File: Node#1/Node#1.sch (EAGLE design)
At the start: 5 parts, among them U1 BLUENRG-232

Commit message: Modified Lib, Node#1
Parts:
- added C10, C4, C5, C6, C7, C8, C9: (no value), rcl:C-EUC0805K
- added C11: (no value), rcl:C-EUC0805
- added D1: BAS40-06, diode:BAS40-06
- added R1, R2: (no value), rcl:R-EU_R0805
- added S1: FSM4JSMAATR, BlueHome:FSM4JSMAATR
- added U$2: SWITCH_L, BlueHome:SWITCH_L
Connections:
- new net N$1: C7.1, C8.1, U1.VDD1V2
- new net N$2: C10.1, C9.1, U$2.1, U1.SMPSFILT1
- new net N$3: C11.2, D1.AA, R1.1, S1.3, S1.4, U1.RESETN
- new net N$5: C11.1, R2.1, S1.1, S1.2
- new net SMPSFILT2: U$2.2, U1.SMPSFILT2
- net +3V3: now also C4.1, C5.1, C6.1, D1.K2, R1.2, U$2.3
- net 0V: now also C10.2, C4.2, C5.2, C6.2, C7.2, C8.2, C9.2, R2.2; no longer U1.VDD1V2
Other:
- moved on the sheet: C1, C2, C3

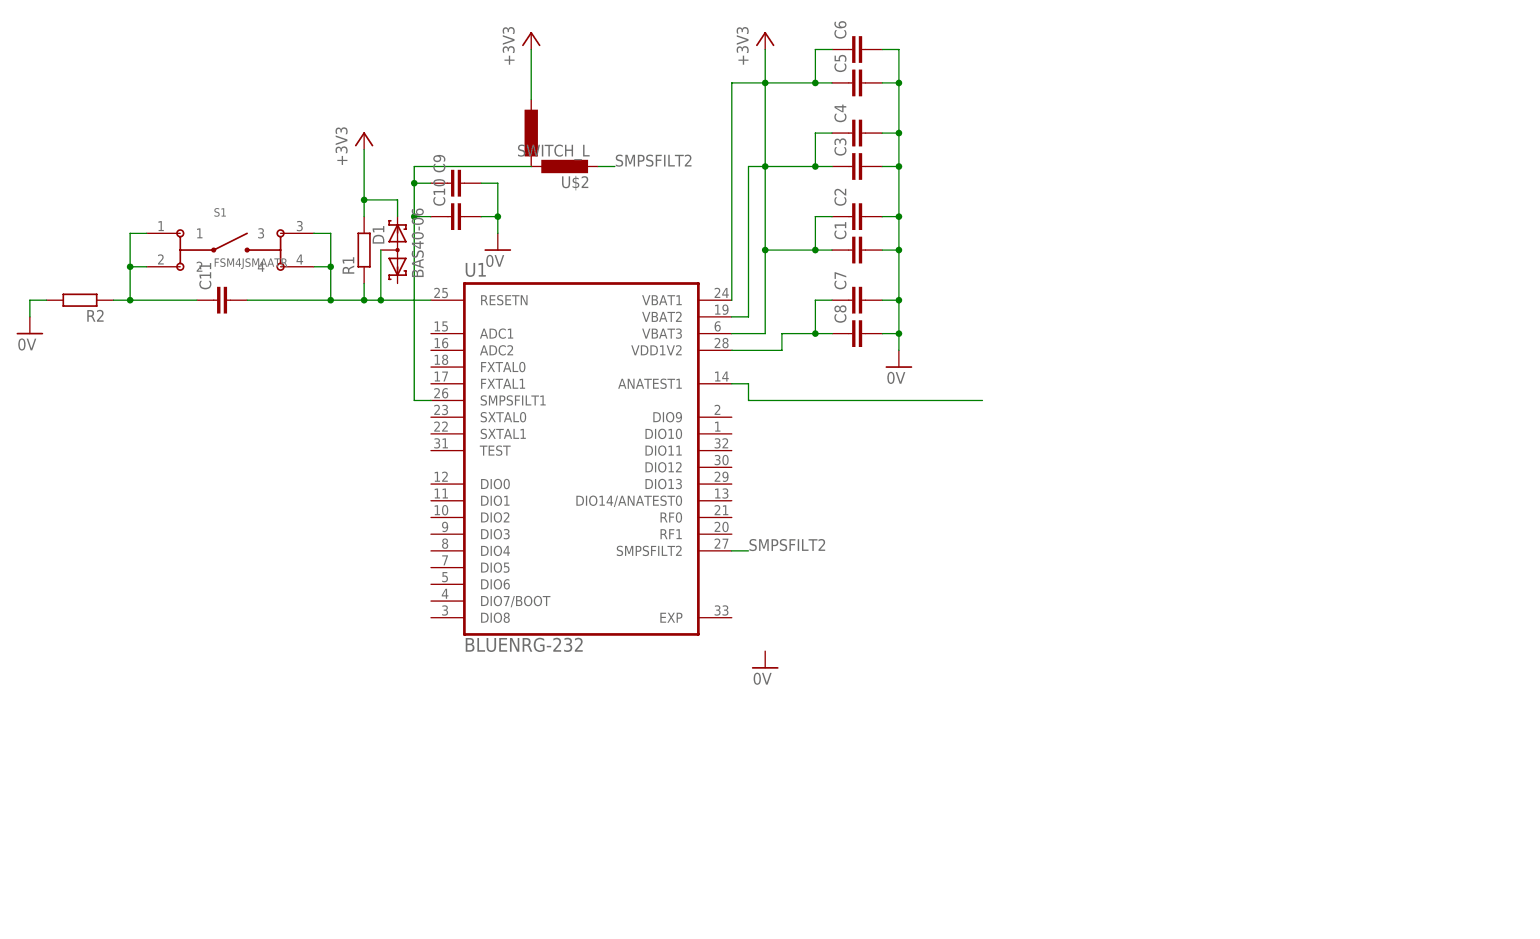
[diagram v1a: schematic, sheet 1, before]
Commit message: Modified library, Node #1 BlueNRG
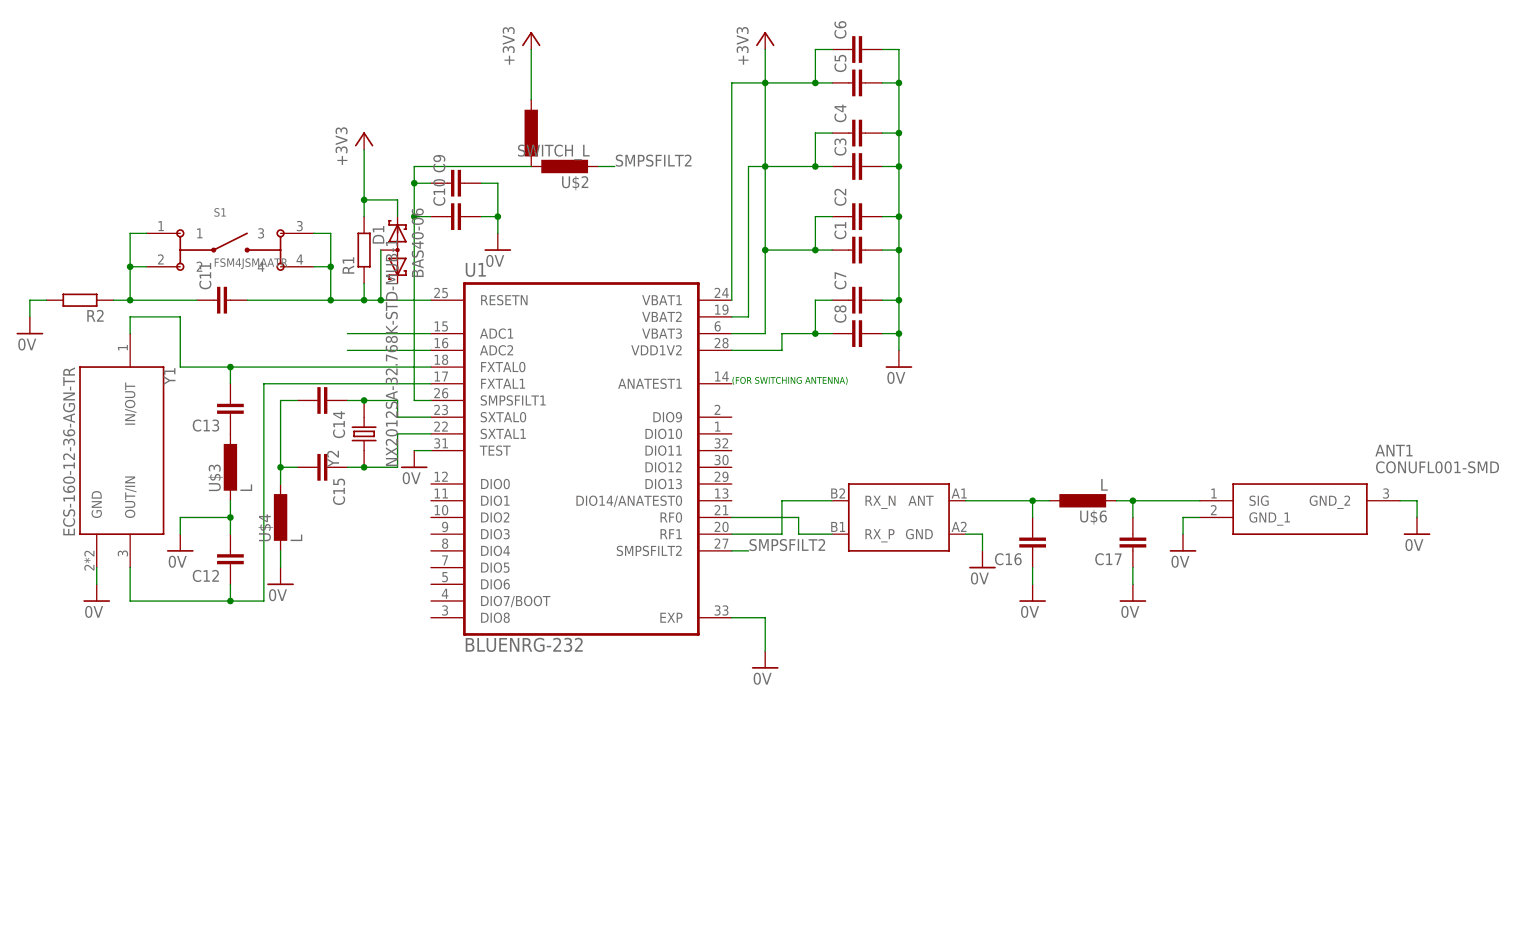
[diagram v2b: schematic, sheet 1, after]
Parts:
- added ANT1: CONUFL001-SMD, BlueHome:CONUFL001-SMD
- added C12, C13, C14, C15, C16, C17: (no value), rcl:C-EUC0805
- added U$3, U$4, U$6: L, BlueHome:L
- added U$5: BALF-NRG-01D3, BlueHome:BALF-NRG-01D3
- added Y1: ECS-160-12-36-AGN-TR, BlueHome:ECS-160-12-36-AGN-TR
- added Y2: NX2012SA-32.768K-STD-MUB-1, BlueHome:NX2012SA-32.768K-STD-MUB-1
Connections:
- new net N$10: C14.1, U1.SXTAL0, Y2.2
- new net N$11: C15.1, U1.SXTAL1, Y2.1
- new net N$12: U1.ADC1
- new net N$13: U1.ADC2
- new net N$14: U$5.RX_N, U1.RF1
- new net N$16: C16.2, U$5.ANT, U$6.1
- new net N$17: ANT1.SIG, C17.2, U$6.2
- new net N$4: C12.1, U1.FXTAL1, Y1.OUT/IN
- new net N$6: C13.2, U1.FXTAL0, Y1.IN/OUT
- new net N$8: C13.1, U$3.1
- new net N$9: C14.2, C15.2, U$4.1
- net 0V: now also ANT1.GND_1, ANT1.GND_2, C12.2, C16.1, C17.1, U$3.2, U$4.2, U$5.GND, U1.EXP, U1.TEST, Y1.GND
- net N$7: now also U$5.RX_P, U1.RF0; no longer U1.ANATEST1
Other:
- note added: "(FOR SWITCHING ANTENNA)"

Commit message: Modified Node#1
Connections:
- new net RXD: U1.DIO11
- new net SCL: U1.DIO4
- new net SDA: U1.DIO5
- new net TXD: U1.DIO8
- net 0V: now also C11.1
- net N$5: no longer C11.1
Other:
- moved on the sheet: R2
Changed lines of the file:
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@@
 <instance part="+3V3" gate="G$1" x="5.08" y="99.06"/>
 <instance part="C11" gate="G$1" x="-17.78" y="73.66" rot="R90"/>
-<instance part="R2" gate="G$1" x="-38.1" y="73.66" rot="R180"/>
+<instance part="R2" gate="G$1" x="-38.1" y="78.74" rot="R180"/>
 <instance part="S1" gate="G$1" x="-15.24" y="81.28"/>
 <instance part="GND4" gate="1" x="-45.72" y="68.58"/>
@@
 <pinref part="GND4" gate="1" pin="0V"/>
 <wire x1="-45.72" y1="71.12" x2="-45.72" y2="73.66" width="0.1524" layer="91"/>
+<pinref part="C11" gate="G$1" pin="1"/>
+<wire x1="-20.32" y1="73.66" x2="-45.72" y2="73.66" width="0.1524" layer="91"/>
+<wire x1="-45.72" y1="73.66" x2="-45.72" y2="78.74" width="0.1524" layer="91"/>
+<junction x="-45.72" y="73.66"/>
 <pinref part="R2" gate="G$1" pin="2"/>
-<wire x1="-45.72" y1="73.66" x2="-43.18" y2="73.66" width="0.1524" layer="91"/>
+<wire x1="-45.72" y1="78.74" x2="-43.18" y2="78.74" width="0.1524" layer="91"/>
 </segment>
 <segment>
@@
 <net name="N$5" class="0">
 <segment>
-<pinref part="C11" gate="G$1" pin="1"/>
-<wire x1="-20.32" y1="73.66" x2="-30.48" y2="73.66" width="0.1524" layer="91"/>
-<wire x1="-30.48" y1="73.66" x2="-30.48" y2="78.74" width="0.1524" layer="91"/>
 <pinref part="S1" gate="G$1" pin="2"/>
 <wire x1="-30.48" y1="78.74" x2="-27.94" y2="78.74" width="0.1524" layer="91"/>
 <wire x1="-30.48" y1="78.74" x2="-30.48" y2="83.82" width="0.1524" layer="91"/>
-<junction x="-30.48" y="78.74"/>
 <pinref part="S1" gate="G$1" pin="1"/>
 <wire x1="-30.48" y1="83.82" x2="-27.94" y2="83.82" width="0.1524" layer="91"/>
 <pinref part="R2" gate="G$1" pin="1"/>
-<wire x1="-33.02" y1="73.66" x2="-30.48" y2="73.66" width="0.1524" layer="91"/>
-<junction x="-30.48" y="73.66"/>
+<wire x1="-33.02" y1="78.74" x2="-30.48" y2="78.74" width="0.1524" layer="91"/>
+<junction x="-30.48" y="78.74"/>
 </segment>
 </net>
@@
 </segment>
 </net>
+<net name="SCL" class="0">
+<segment>
+<pinref part="U1" gate="G$1" pin="DIO4"/>
+<wire x1="15.24" y1="35.56" x2="7.62" y2="35.56" width="0.1524" layer="91"/>
+<label x="7.62" y="35.56" size="1.778" layer="95"/>
+</segment>
+</net>
+<net name="SDA" class="0">
+<segment>
+<pinref part="U1" gate="G$1" pin="DIO5"/>
+<wire x1="15.24" y1="33.02" x2="7.62" y2="33.02" width="0.1524" layer="91"/>
+<label x="7.62" y="33.02" size="1.778" layer="95"/>
+</segment>
+</net>
+<net name="TXD" class="0">
+<segment>
+<pinref part="U1" gate="G$1" pin="DIO8"/>
+<wire x1="15.24" y1="25.4" x2="7.62" y2="25.4" width="0.1524" layer="91"/>
+<label x="7.62" y="25.4" size="1.778" layer="95"/>
+</segment>
+</net>
+<net name="RXD" class="0">
+<segment>
+<pinref part="U1" gate="G$1" pin="DIO11"/>
+<wire x1="60.96" y1="50.8" x2="66.04" y2="50.8" width="0.1524" layer="91"/>
+<label x="66.04" y="50.8" size="1.778" layer="95"/>
+</segment>
+</net>

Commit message: Finished BlueNRG
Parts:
- added JP1: (no value), pinhead:PINHD-2X5
- added R3, R4: (no value), rcl:R-EU_R0805
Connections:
- net N$12 renamed ADC1
- net N$13 renamed ADC2
- new net DIO0: U1.DIO0
- new net DIO1: U1.DIO1
- new net DIO12: U1.DIO12
- new net DIO13: U1.DIO13
- new net DIO14: U1.DIO14/ANATEST0
- new net DIO2: U1.DIO2
- new net DIO3: U1.DIO3
- new net DIO6: U1.DIO6
- new net DIO7: U1.DIO7/BOOT
- new net JTCK: U1.DIO9
- new net JTMS: U1.DIO10
- net +3V3: now also R3.2, R4.2
- net SCL: now also R3.1
- net SDA: now also R4.1
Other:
- note added: "JTAG"
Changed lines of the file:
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@@
 <part name="GND12" library="supply1" deviceset="0V" device=""/>
 <part name="GND13" library="supply1" deviceset="0V" device=""/>
+<part name="R3" library="rcl" deviceset="R-EU_" device="R0805"/>
+<part name="R4" library="rcl" deviceset="R-EU_" device="R0805"/>
+<part name="+3V4" library="supply1" deviceset="+3V3" device=""/>
+<part name="JP1" library="pinhead" deviceset="PINHD-2X5" device=""/>
 </parts>
 <sheets>
@@
 <plain>
 <text x="60.96" y="60.96" size="1.016" layer="91">(FOR SWITCHING ANTENNA)</text>
+<text x="30.48" y="-12.7" size="1.778" layer="91">JTAG</text>
 </plain>
 <instances>
@@
 <instance part="U$4" gate="G$1" x="-7.62" y="40.64"/>
 <instance part="GND7" gate="1" x="-7.62" y="30.48"/>
-<instance part="GND8" gate="1" x="12.7" y="48.26"/>
+<instance part="GND8" gate="1" x="12.7" y="50.8" rot="R270"/>
 <instance part="U$5" gate="A" x="86.36" y="40.64"/>
 <instance part="GND9" gate="1" x="99.06" y="33.02"/>
@@
 <instance part="GND12" gate="1" x="129.54" y="35.56"/>
 <instance part="GND13" gate="1" x="165.1" y="38.1"/>
+<instance part="R3" gate="G$1" x="7.62" y="35.56" rot="R180"/>
+<instance part="R4" gate="G$1" x="7.62" y="33.02" rot="R180"/>
+<instance part="+3V4" gate="G$1" x="0" y="40.64"/>
+<instance part="JP1" gate="A" x="35.56" y="-2.54"/>
 </instances>
 <busses>
@@
 <junction x="5.08" y="88.9"/>
 </segment>
+<segment>
+<pinref part="R4" gate="G$1" pin="2"/>
+<wire x1="2.54" y1="33.02" x2="0" y2="33.02" width="0.1524" layer="91"/>
+<pinref part="+3V4" gate="G$1" pin="+3V3"/>
+<wire x1="0" y1="33.02" x2="0" y2="35.56" width="0.1524" layer="91"/>
+<pinref part="R3" gate="G$1" pin="2"/>
+<wire x1="0" y1="35.56" x2="0" y2="38.1" width="0.1524" layer="91"/>
+<wire x1="2.54" y1="35.56" x2="0" y2="35.56" width="0.1524" layer="91"/>
+<junction x="0" y="35.56"/>
+</segment>
 </net>
 <net name="0V" class="0">
@@
 <pinref part="U1" gate="G$1" pin="TEST"/>
 <pinref part="GND8" gate="1" pin="0V"/>
-<wire x1="15.24" y1="50.8" x2="12.7" y2="50.8" width="0.1524" layer="91"/>
 </segment>
 <segment>
@@
 </segment>
 </net>
-<net name="N$12" class="0">
+<net name="ADC1" class="0">
 <segment>
 <pinref part="U1" gate="G$1" pin="ADC1"/>
 <wire x1="15.24" y1="68.58" x2="2.54" y2="68.58" width="0.1524" layer="91"/>
-</segment>
-</net>
-<net name="N$13" class="0">
+<label x="0" y="68.58" size="1.778" layer="95"/>
+</segment>
+</net>
+<net name="ADC2" class="0">
 <segment>
 <pinref part="U1" gate="G$1" pin="ADC2"/>
 <wire x1="15.24" y1="66.04" x2="2.54" y2="66.04" width="0.1524" layer="91"/>
+<label x="0" y="66.04" size="1.778" layer="95"/>
 </segment>
 </net>
@@
 <segment>
 <pinref part="U1" gate="G$1" pin="DIO4"/>
-<wire x1="15.24" y1="35.56" x2="7.62" y2="35.56" width="0.1524" layer="91"/>
-<label x="7.62" y="35.56" size="1.778" layer="95"/>
+<wire x1="15.24" y1="35.56" x2="12.7" y2="35.56" width="0.1524" layer="91"/>
+<label x="12.7" y="35.56" size="1.778" layer="95"/>
+<pinref part="R3" gate="G$1" pin="1"/>
 </segment>
 </net>
@@
 <segment>
 <pinref part="U1" gate="G$1" pin="DIO5"/>
-<wire x1="15.24" y1="33.02" x2="7.62" y2="33.02" width="0.1524" layer="91"/>
-<label x="7.62" y="33.02" size="1.778" layer="95"/>
+<wire x1="15.24" y1="33.02" x2="12.7" y2="33.02" width="0.1524" layer="91"/>
+<label x="12.7" y="33.02" size="1.778" layer="95"/>
+<pinref part="R4" gate="G$1" pin="1"/>
 </segment>
 </net>
@@
 <segment>
 <pinref part="U1" gate="G$1" pin="DIO8"/>
-<wire x1="15.24" y1="25.4" x2="7.62" y2="25.4" width="0.1524" layer="91"/>
-<label x="7.62" y="25.4" size="1.778" layer="95"/>
+<wire x1="15.24" y1="25.4" x2="10.16" y2="25.4" width="0.1524" layer="91"/>
+<label x="10.16" y="25.4" size="1.778" layer="95"/>
 </segment>
 </net>
@@
 <pinref part="U1" gate="G$1" pin="DIO11"/>
 <wire x1="60.96" y1="50.8" x2="66.04" y2="50.8" width="0.1524" layer="91"/>
-<label x="66.04" y="50.8" size="1.778" layer="95"/>
-</segment>
-</net>
+<label x="63.5" y="50.8" size="1.778" layer="95"/>
+</segment>
+</net>
+<net name="DIO0" class="0">
+<segment>
+<pinref part="U1" gate="G$1" pin="DIO0"/>
+<wire x1="15.24" y1="45.72" x2="10.16" y2="45.72" width="0.1524" layer="91"/>
+<label x="5.08" y="45.72" size="1.778" layer="95"/>
+</segment>
+</net>
+<net name="DIO1" class="0">
+<segment>
+<pinref part="U1" gate="G$1" pin="DIO1"/>
+<wire x1="15.24" y1="43.18" x2="10.16" y2="43.18" width="0.1524" layer="91"/>
+<label x="5.08" y="43.18" size="1.778" layer="95"/>
+</segment>
+</net>
+<net name="DIO2" class="0">
+<segment>
+<pinref part="U1" gate="G$1" pin="DIO2"/>
+<wire x1="15.24" y1="40.64" x2="10.16" y2="40.64" width="0.1524" layer="91"/>
+<label x="5.08" y="40.64" size="1.778" layer="95"/>
+</segment>
+</net>
+<net name="DIO3" class="0">
+<segment>
+<pinref part="U1" gate="G$1" pin="DIO3"/>
+<wire x1="15.24" y1="38.1" x2="10.16" y2="38.1" width="0.1524" layer="91"/>
+<label x="5.08" y="38.1" size="1.778" layer="95"/>
+</segment>
+</net>
+<net name="DIO6" class="0">
+<segment>
+<pinref part="U1" gate="G$1" pin="DIO6"/>
+<wire x1="15.24" y1="30.48" x2="10.16" y2="30.48" width="0.1524" layer="91"/>
+<label x="5.08" y="30.48" size="1.778" layer="95"/>
+</segment>
+</net>
+<net name="DIO7" class="0">
+<segment>
+<pinref part="U1" gate="G$1" pin="DIO7/BOOT"/>
+<wire x1="15.24" y1="27.94" x2="10.16" y2="27.94" width="0.1524" layer="91"/>
+<label x="5.08" y="27.94" size="1.778" layer="95"/>
+</segment>
+</net>
+<net name="JTCK" class="0">
+<segment>
+<pinref part="U1" gate="G$1" pin="DIO9"/>
+<wire x1="60.96" y1="55.88" x2="66.04" y2="55.88" width="0.1524" layer="91"/>
+<label x="63.5" y="55.88" size="1.778" layer="95"/>
+</segment>
+</net>
+<net name="JTMS" class="0">
+<segment>
+<pinref part="U1" gate="G$1" pin="DIO10"/>
+<wire x1="60.96" y1="53.34" x2="66.04" y2="53.34" width="0.1524" layer="91"/>
+<label x="63.5" y="53.34" size="1.778" layer="95"/>
+</segment>
+</net>
+<net name="DIO12" class="0">
+<segment>
+<pinref part="U1" gate="G$1" pin="DIO12"/>
+<wire x1="60.96" y1="48.26" x2="66.04" y2="48.26" width="0.1524" layer="91"/>
+<label x="63.5" y="48.26" size="1.778" layer="95"/>
+</segment>
+</net>
+<net name="DIO13" class="0">
+<segment>
+<pinref part="U1" gate="G$1" pin="DIO13"/>
+<wire x1="60.96" y1="45.72" x2="66.04" y2="45.72" width="0.1524" layer="91"/>
+<label x="63.5" y="45.72" size="1.778" layer="95"/>
+</segment>
+</net>
+<net name="DIO14" class="0">
+<segment>
+<pinref part="U1" gate="G$1" pin="DIO14/ANATEST0"/>
+<wire x1="60.96" y1="43.18" x2="66.04" y2="43.18" width="0.1524" layer="91"/>
+<label x="63.5" y="43.18" size="1.778" layer="95"/>
+</segment>
+</net>

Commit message: Finished BlueNRG 2; Added IO-Expander
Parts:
- removed U$2: SWITCH_L, BlueHome:SWITCH_L
- added D2, D3, D4, D5, D6, D7, D8, D9: BAS40-06, diode:BAS40-06
- added JMP1: 0R-JUMPA, jump-0r-smd:0R-JUMPA
- added JP2: (no value), jumper:JP1E
- added JP3, JP5: (no value), jumper:JP2E
- added JP4: (no value), pinhead:PINHD-1X3
- added LED1, LED10, LED11, LED12, LED13, LED14, LED15, LED16, LED2, LED3, LED4, LED5, LED6, LED7, LED8, LED9: (no value), led:LED3MM
- added R10, R11, R12, R13, R14, R15, R16, R17, R18, R19, R20, R21, R22, R23, R24, R25, R26, R27, R28, R29, R30, R31, R32, R33, R34, R35, R36, R37, R38, R5, R6, R7, R8, R9: (no value), rcl:R-EU_R0805
- added U2: SEMTECH_SX1503I091TRTSEMTECH_SX1503I091TRT_0_0, BlueHome:SEMTECH_SX1503I091TRTSEMTECH_SX1503I091TRT_0_0
- added X1, X3: 2081-1228, BlueHome:2081-1228
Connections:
- new net +5V: JP3.3, JP5.3
- new net GND: ANT1.GND_1, ANT1.GND_2, C1.2, C10.2, C11.1, C16.1, C17.1, C2.2, C3.2, C4.2, C5.2, C6.2, C7.2, C8.2, C9.2, D2.AA, D3.AA, D4.AA, D5.AA, D6.AA, D7.AA, D8.AA, D9.AA, JP1.3, JP1.5, JP1.9, JP4.3, LED1.C, LED10.C, LED11.C, LED12.C, LED13.C, LED14.C, LED15.C, LED16.C, LED2.C, LED3.C, LED4.C, LED5.C, LED6.C, LED7.C, LED8.C, LED9.C, R2.2, U$4.2, U$5.GND, U1.EXP, U1.TEST, U2.1_GND, U2.2_GND, U2.3_GND, U2.4_GND, U2.5_GND, Y1.GND
- new net N$12: JP3.2, U2.VCC1
- new net N$13: JP5.2, U2.VCC2
- new net N$15: D2.K1, R7.2, R8.2, U2.I/O[0]
- new net N$18: R9.1, X1.P7
- new net N$19: LED9.A, R10.2
- new net N$20: D3.K2, R13.2, R14.1, U2.I/O[3]
- new net N$21: D4.K1, R15.2, R16.2, U2.I/O[4]
- new net N$22: D4.K2, R17.2, R18.1, U2.I/O[5]
- new net N$23: D6.K2, R25.2, R26.1, U2.I/O[9]
- new net N$24: R13.1, X1.P5
- new net N$25: D6.K1, R23.2, R24.2, U2.I/O[8]
- new net N$27: D7.K1, R27.2, R28.2, U2.I/O[10]
- new net N$28: D7.K2, R29.2, R30.1, U2.I/O[11]
- new net N$29: D8.K1, R31.2, R32.2, U2.I/O[12]
- new net N$30: D8.K2, R33.2, R34.1, U2.I/O[13]
- new net N$31: D9.K1, R35.2, R36.2, U2.I/O[14]
- new net N$32: D9.K2, R37.2, R38.1, U2.I/O[15]
- new net N$33: LED1.A, R7.1
- new net N$34: R25.1, X3.P7
- new net N$35: D2.K2, R10.1, R9.2, U2.I/O[1]
- new net N$36: R8.1, X1.P8
- new net N$37: D3.K1, R11.2, R12.2, U2.I/O[2]
- new net N$38: LED10.A, R11.1
- new net N$40: R12.1, X1.P6
- new net N$41: LED11.A, R14.2
- new net N$42: R17.1, X1.P3
- new net N$43: LED12.A, R15.1
- new net N$45: R16.1, X1.P4
- new net N$46: LED13.A, R18.2
- new net N$47: D5.K1, R19.2, R20.2, U2.I/O[6]
- new net N$48: R21.1, X1.P1
- new net N$49: LED14.A, R19.1
- new net N$50: D5.K2, R21.2, R22.1, U2.I/O[7]
- new net N$51: R20.1, X1.P2
- new net N$52: LED15.A, R22.2
- new net N$54: LED2.A, R23.1
- new net N$56: R24.1, X3.P8
- new net N$58: LED3.A, R26.2
- new net N$59: R29.1, X3.P5
- new net N$60: LED4.A, R27.1
- new net N$61: R28.1, X3.P6
- new net N$62: LED5.A, R30.2
- new net N$63: R33.1, X3.P3
- new net N$64: LED6.A, R31.1
- new net N$65: R32.1, X3.P4
- new net N$66: LED7.A, R34.2
- new net N$68: R37.1, X3.P1
- new net N$69: LED8.A, R35.1
- new net N$71: R36.1, X3.P2
- new net N$72: LED16.A, R38.2
- new net RESETN: C11.2, D1.AA, JP1.10, R1.1, S1.3, S1.4, U1.RESETN, U2.!RESET!
- new net TDI: JP1.8, R5.1, U1.DIO0
- new net TDO: JP1.6, R6.1, U1.DIO1
- net +3V3: now also JMP1-0R.3, JP2.2, JP3.1, JP5.1, U2.VDDM; no longer U$2.3
- net 0V: no longer ANT1.GND_1, ANT1.GND_2, C1.2, C10.2, C11.1, C16.1, C17.1, C2.2, C3.2, C4.2, C5.2, C6.2, C7.2, C8.2, C9.2, R2.2, U$4.2, U$5.GND, U1.EXP, U1.TEST, Y1.GND
- net DIO0: now also R5.2; no longer U1.DIO0
- net DIO1: now also R6.2; no longer U1.DIO1
- net JTCK: now also JP1.4
- net JTMS: now also JP1.2
- net N$2: now also JMP1-0R.2; no longer U$2.1
- net N$3: now also JP1.1, JP2.1; no longer C11.2, D1.AA, R1.1, S1.3, S1.4, U1.RESETN
- net RXD: now also JP4.2
- net SCL: now also U2.SCL
- net SDA: now also U2.SDA
- net SMPSFILT2: now also JMP1-0R.1; no longer U$2.2
- net TXD: now also JP4.1
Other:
- note added: "9 IO"
- note added: "ARM 10-PIN Interface"
- note added: "Serial"
